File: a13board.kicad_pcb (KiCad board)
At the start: 4 copper layers, 123.5 x 91.1 mm, 152 parts, among them P1 CONN_20, P2 CONN_20, P3 CONN_20, P4 CONN_20, P5 CONN_20, U1 H27UBG8T2A/TSOP48, U2 A13, U3 H5TQ2G43CFR, U4 H5TQ2G43CFR, U5 OLIMEX_IC_AXP209, U6 SY8008BAAC, U7 SY8008BAAC

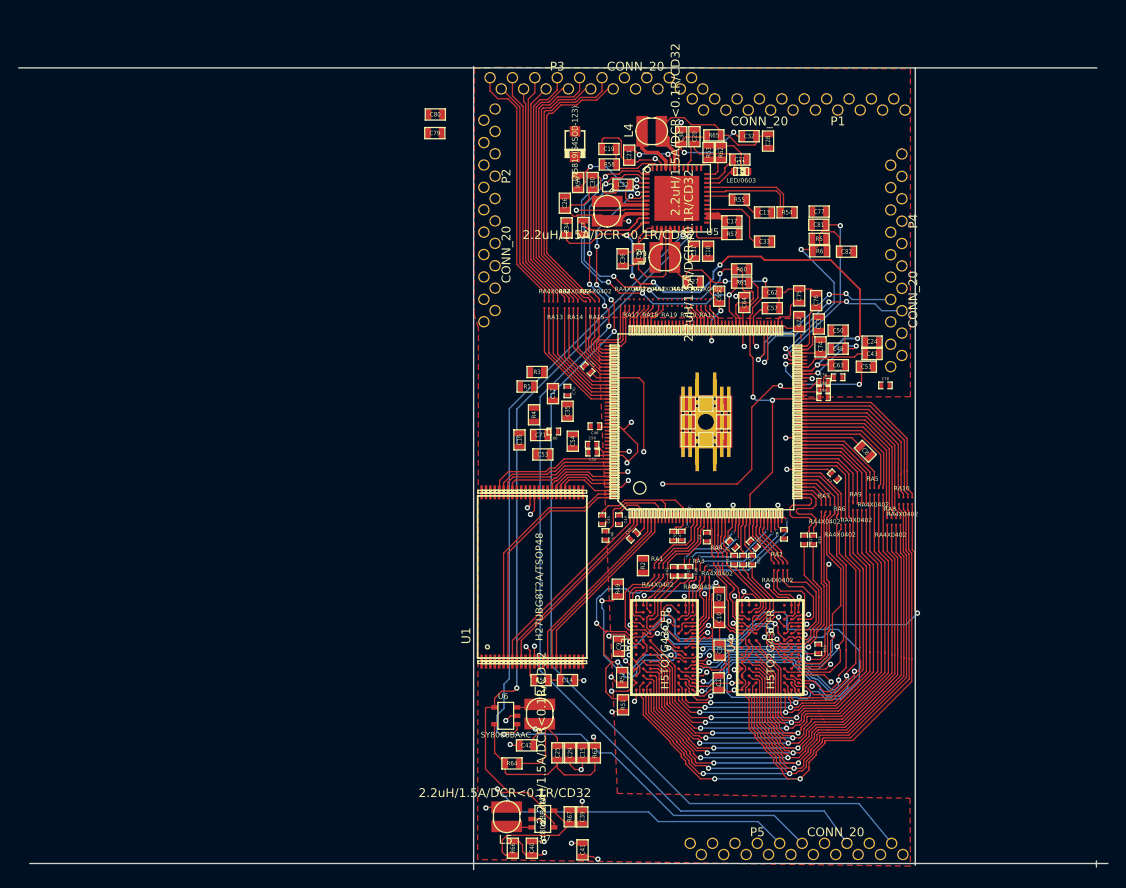
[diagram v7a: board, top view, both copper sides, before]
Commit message: Connected a few more connections; BGA escape finished
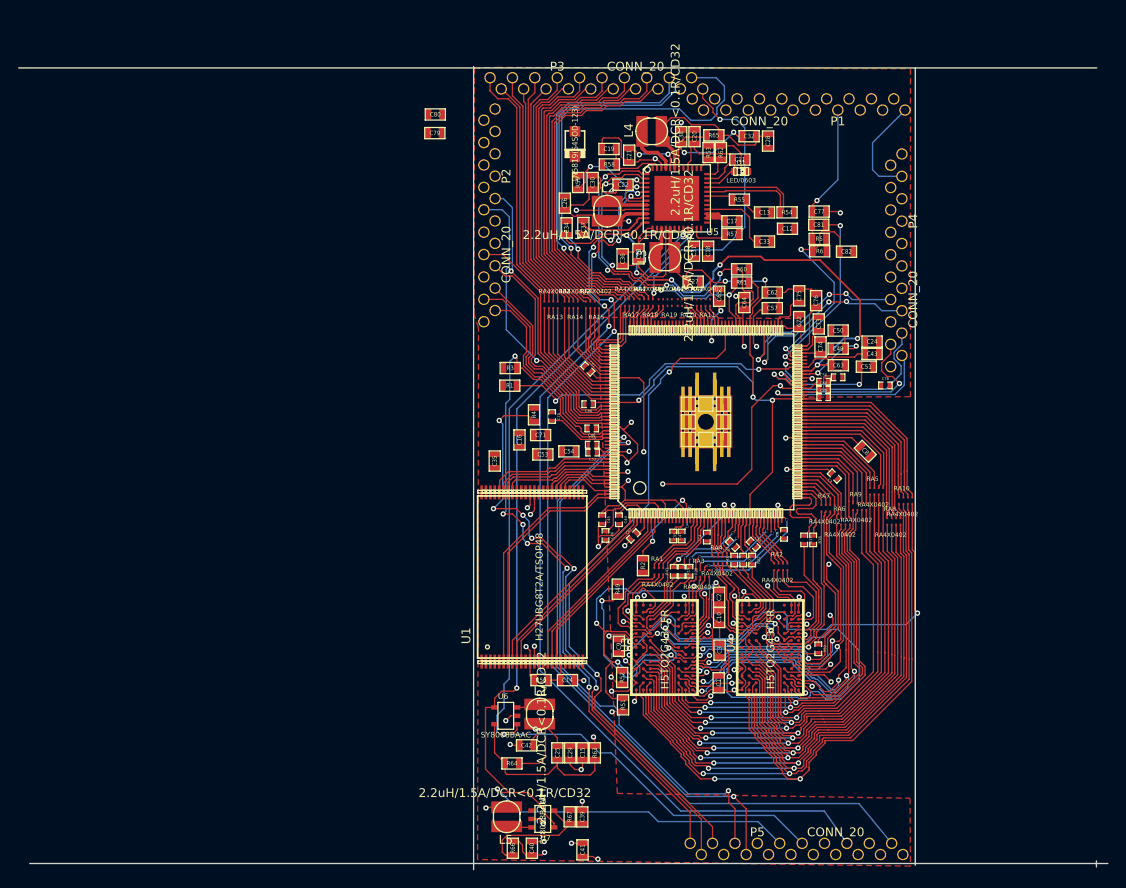
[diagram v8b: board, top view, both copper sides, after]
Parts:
- moved C12 32.5 mm to (122.8, 69.1), turned to 0 degrees
- moved C35 10.00 mm to (89.5, 95.5)
- moved C66 5.02 mm to (100.2, 89.0)
- moved C70 3.38 mm to (96.0, 90.4)
- moved R3 3.08 mm to (91.3, 84.9)
- moved R1 1.97 mm to (91.2, 86.9)
- moved C54 1.23 mm to (98.0, 94.3), turned to 0 degrees
- moved C48 0.43 mm to (100.5, 91.8)
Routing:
- net NMI_N: track 0.00 -> 83.0 mm, vias 0 -> 6
- net PB15: track 0.00 -> 75.8 mm, vias 0 -> 2
- net RESET: track 0.00 -> 75.1 mm, vias 0 -> 6
- net PB18: track 0.00 -> 65.1 mm, vias 0 -> 2
- net PB17: track 0.00 -> 63.7 mm, vias 0 -> 2
- net PD24: track 0.00 -> 53.3 mm, vias 0 -> 1
- net PD22: track 0.00 -> 42.2 mm, vias 0 -> 1
- net PD23: track 0.00 -> 41.8 mm, vias 0 -> 1
- net PD20: track 0.00 -> 38.8 mm
- net PD21: track 0.00 -> 38.4 mm
- net PD18: track 0.00 -> 36.9 mm
- net PD19: track 0.00 -> 36.4 mm
- net N-00000185: track 9.35 -> 45.0 mm, vias 0 -> 2
- net PD25: track 0.00 -> 34.1 mm, vias 0 -> 2
- net PG3: track 0.00 -> 33.2 mm, vias 0 -> 1
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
